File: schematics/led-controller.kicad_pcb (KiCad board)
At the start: 2 copper layers, 58 parts, among them IC1 ATMEGA168A-P, P1 CONN_01X03, P2 CONN_01X03, P3 CONN_01X02, P4 CONN_01X02, P5 CONN_01X02, P6 CONN_01X02, P7 ISP, P8 COM, Q1 IRLU 120N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

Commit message: first checked version
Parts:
- removed JP1: Jumper_NO_Small, Pin_Headers:Pin_Header_Straight_1x02
- added C10: 100n, Capacitors_ThroughHole:C_Rect_L7_W2.5_P5, F.Cu at (103.9, 101.9)
- added C11: 100n, Capacitors_ThroughHole:C_Rect_L7_W2.5_P5, F.Cu at (158.0, 74.2)
- added CON1: BARREL_JACK, Connect:BARREL_JACK, F.Cu at (172.5, 105.4)
- added D6: 1N5408, Diodes_ThroughHole:Diode_DO-201AD_Horizontal_RM15, F.Cu at (176.3, 87.4)
- added F1: 3A, Fuse_Holders_and_Fuses:Fuseholder5x20_horiz_open_lateral_Type-II, F.Cu at (168.4, 85.1)
- added REF**: MountingHole_3.2mm_M3, Mounting_Holes:MountingHole_3.2mm_M3, F.Cu at (99.1, 121.9)
- added REF**: MountingHole_3.2mm_M3, Mounting_Holes:MountingHole_3.2mm_M3, F.Cu at (99.1, 38.1)
- added REF**: MountingHole_3.2mm_M3, Mounting_Holes:MountingHole_3.2mm_M3, F.Cu at (172.7, 38.1)
- added REF**: MountingHole_3.2mm_M3, Mounting_Holes:MountingHole_3.2mm_M3, F.Cu at (172.7, 121.9)
- C1, C2, C3, C4: footprint Capacitors_ThroughHole:C_Radial_D5_L11_P2.5 -> Capacitors_ThroughHole:C_Radial_D8_L11.5_P3.5
- P1: value CONN_01X03 -> VIN
- P2: value CONN_01X03 -> VOUT
- P3: value CONN_01X02 -> LED1; footprint Connect:AK300-2 -> Connect:bornier2
- P4, P5, P6: footprint Connect:AK300-2 -> Connect:bornier2
- P7: footprint Socket_Strips:Socket_Strip_Straight_2x03 -> Pin_Headers:Pin_Header_Straight_2x03
- RR4: value 20k -> 27k
- RV1, RV2, RV3, RV4: footprint Potentiometers:Potentiometer_Trimmer-Suntan-TSR-3386C -> Trimmers:Potentiometer_Trimmer-Suntan-TSR-3296
- U3: value LF33CV -> LP 2950 ACZ3,3; footprint TO_SOT_Packages_THT:TO-220_Neutral123_Vertical -> TO_SOT_Packages_THT:TO-92_Inline_Narrow_Oval
- moved C5 49.3 mm to (103.9, 80.5)
- moved C7 40.3 mm to (148.1, 102.9), turned to 270 degrees
- moved C6 34.8 mm to (134.9, 77.5), turned to 180 degrees
- moved P1 34.1 mm to (161.0, 117.6), turned to 90 degrees
- moved C8 30.1 mm to (151.6, 108.0), turned to 90 degrees
- moved C9 23.3 mm to (103.9, 112.3), turned to 270 degrees
- moved RR3 15.5 mm to (109.5, 91.4)
- moved P2 14.0 mm to (161.0, 113.3), turned to 90 degrees
- moved P8 4.33 mm to (161.0, 122.7), turned to 90 degrees
- moved C1 3.56 mm to (101.3, 67.1)
- moved Q4 3.56 mm to (173.7, 67.1)
- moved U3 2.59 mm to (156.7, 102.9)
- moved P4 2.55 mm to (126.7, 36.6), turned to 180 degrees
- moved P5 2.55 mm to (145.0, 36.6), turned to 180 degrees
- moved P6 2.55 mm to (163.3, 36.6), turned to 180 degrees
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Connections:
- C6 pad 1: +3V3 -> VCC
- C7 pad 1: +3V3 -> VCC
- IC1 pad 25: SENSE2 -> SENSE1
- IC1 pad 26: SENSE1 -> SENSE2
- P1 pad 2: Net-(JP1-Pad1) -> +3V3
- P2 pad 2: Net-(JP1-Pad1) -> +3V3
- P3 pad 1: /IRAW1 -> Net-(L1-Pad1)
- P3 pad 2: Net-(L1-Pad1) -> /IRAW1
- P4 pad 1: /IRAW2 -> Net-(L2-Pad1)
- P4 pad 2: Net-(L2-Pad1) -> /IRAW2
- P5 pad 1: /IRAW3 -> Net-(L3-Pad1)
- P5 pad 2: Net-(L3-Pad1) -> /IRAW3
- P6 pad 1: /IRAW4 -> Net-(L4-Pad1)
- P6 pad 2: Net-(L4-Pad1) -> /IRAW4
- RR3 pad 2: /PULLUP1 -> /PULLUP2
- RR3 pad 3: /PULLUP2 -> /PULLUP1
- RR3 pad 4: /PULLUP3 -> /PULLUP4
- RR3 pad 5: /PULLUP4 -> /PULLUP3
- U2 pad 1: /PULLUP1 -> (no net)
- U2 pad 10: (no net) -> SENSE1
- U2 pad 11: (no net) -> /PULLUP1
- U2 pad 12: (no net) -> SENSE2
- U2 pad 13: (no net) -> /PULLUP2
- U2 pad 2: SENSE1 -> (no net)
- U2 pad 3: /PULLUP2 -> (no net)
- U2 pad 4: SENSE2 -> (no net)
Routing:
- net Net-(JP1-Pad1): track 58.6 -> 0.00 mm
- net Net-(CON1-Pad1): track 0.00 -> 18.7 mm
- net +3V3: track 135.3 -> 152.8 mm
- net /PULLUP2: track 26.6 -> 9.94 mm
- net Net-(D6-Pad2): track 0.00 -> 12.6 mm
- net /PULLUP1: track 22.4 -> 11.0 mm
- net /PULLUP4: track 34.4 -> 23.1 mm
- net SWITCH4: track 29.3 -> 39.5 mm
- net SENSE2: track 67.3 -> 76.0 mm
- net MOSI: track 12.8 -> 19.5 mm
- net VCC: track 197.5 -> 203.0 mm
- net SCK: track 19.5 -> 14.2 mm
- net SENSE1: track 78.4 -> 82.9 mm
- net SWITCH2: track 39.6 -> 35.9 mm
- net MISO: track 17.6 -> 14.1 mm
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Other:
- board outline added: 88.9 x 97.8 mm
- board text added: "4 Channel LED Driver, (c) Andreas Stöckel, 2016 max. 0.9A per channel, 3A total"
- board text added: "DC IN 5-25V"
- board text added: "RX"
- board text added: "TX"
- board text added: "UART"
- board text added: "VIN"
- board text added: "VOUT"

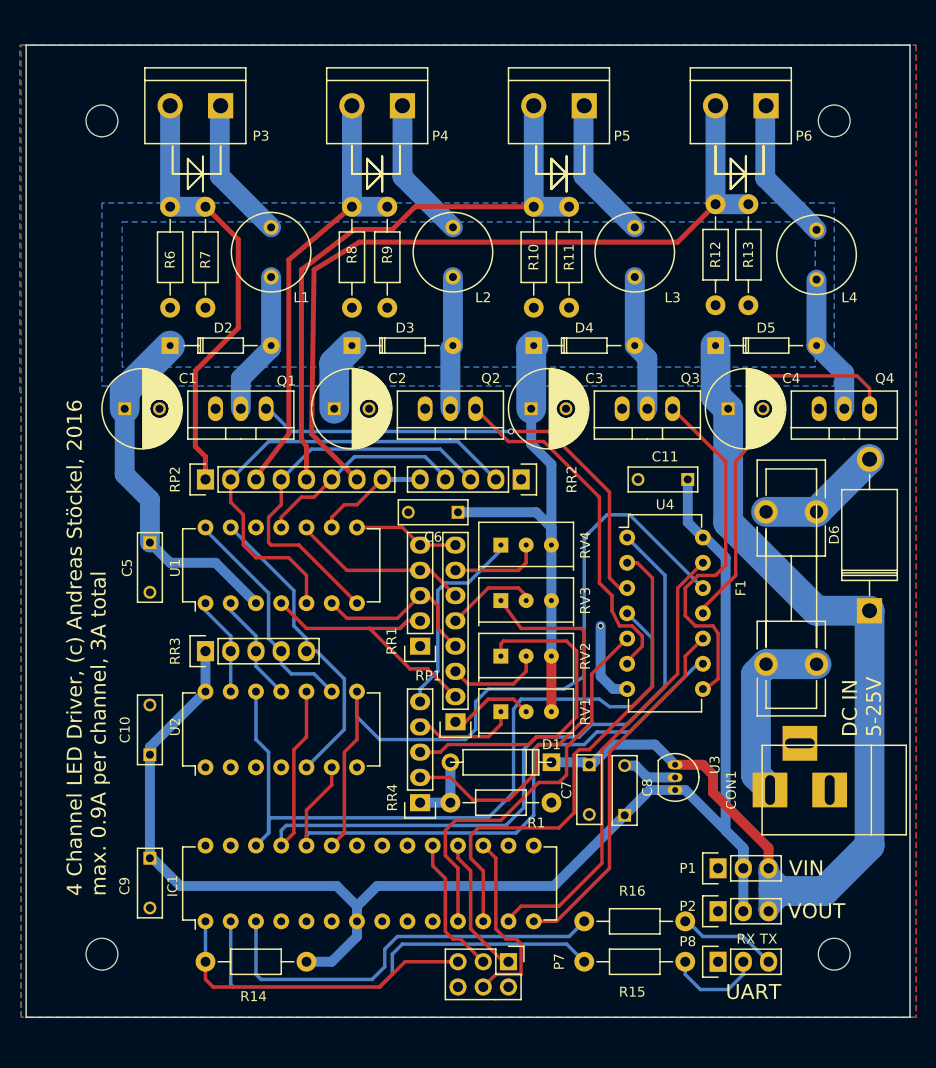
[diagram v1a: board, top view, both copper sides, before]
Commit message: Improve PCB
- Move mounting holes to 71.5mm distance, allows to attach the board to a
  80mm fan
- Improve ground planes, remove one via
- Prettify some tracks
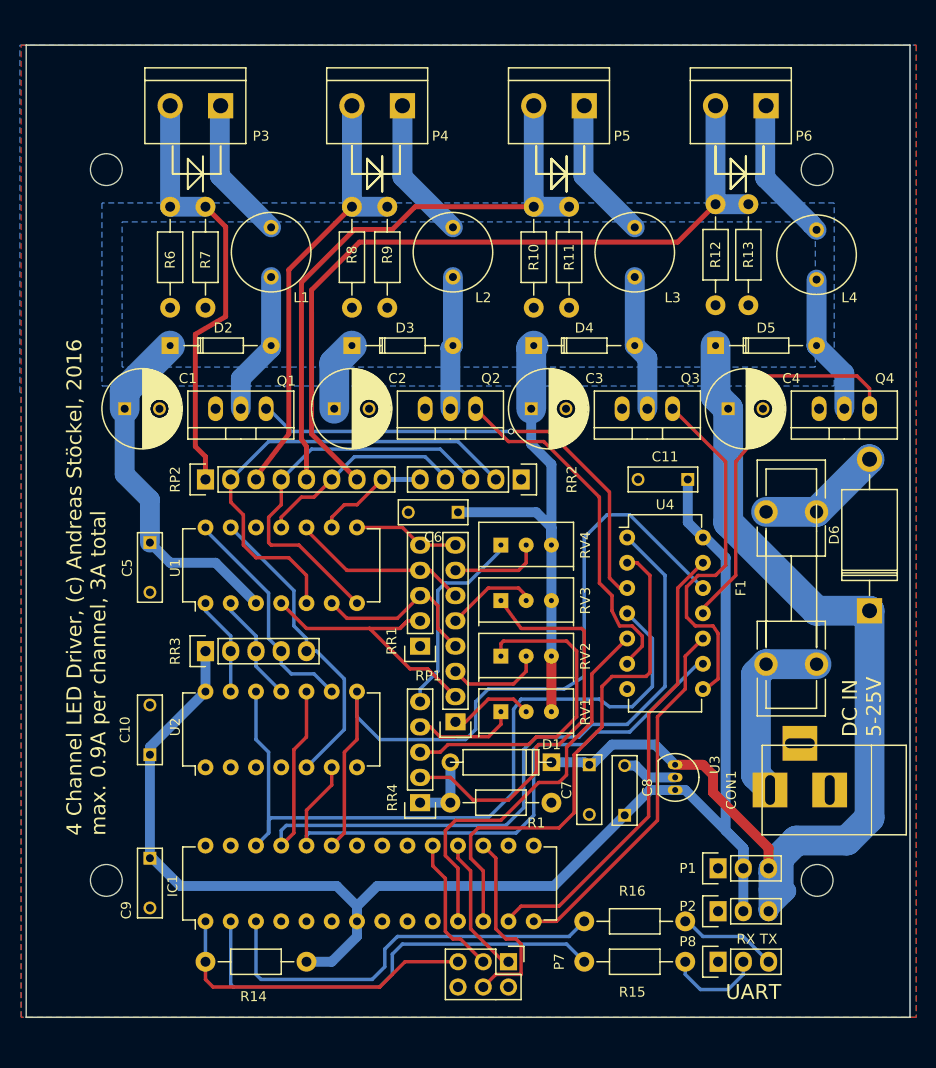
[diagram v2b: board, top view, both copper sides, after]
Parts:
- moved REF** 7.62 mm to (171.0, 114.5)
- moved REF** 7.43 mm to (99.5, 114.5)
- moved REF** 5.19 mm to (171.0, 43.0)
- moved REF** 4.92 mm to (99.5, 43.0)
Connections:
- U2 pad 1: (no net) -> GND
- U2 pad 2: (no net) -> Net-(U2-Pad2)
- U2 pad 3: (no net) -> GND
- U2 pad 4: (no net) -> Net-(U2-Pad4)
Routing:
- net GND: track 13.8 -> 5.57 mm, vias 1 -> 0
- net TRIGGER1: track 51.2 -> 52.5 mm
- net /IRAW4: track 78.7 -> 78.1 mm
- net /IRAW1: track 44.7 -> 44.2 mm
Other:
- board text removed: "VIN"
- board text removed: "VOUT"

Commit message: Board version 1.0 RC1
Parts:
- removed D1: 3V6, Discret:D4
- removed D6: 1N5408, Diodes_ThroughHole:Diode_DO-201AD_Horizontal_RM15
- removed R1: 1k, Resistors_ThroughHole:Resistor_Horizontal_RM10mm
- added C12: 100n, Capacitors_ThroughHole:C_Rect_L7_W2.5_P5, F.Cu at (138.6, 105.5)
- added C13: 100n, Capacitors_ThroughHole:C_Rect_L7_W2.5_P5, F.Cu at (127.3, 105.5)
- added P9: EXPANSION, Pin_Headers:Pin_Header_Straight_1x04, F.Cu at (106.9, 105.5)
- added U5: 7905_wno, TO_SOT_Packages_THT:TO-92_Inline_Narrow_Oval, F.Cu at (124.2, 89.9)
- D2, D3, D4, D5: value SD101C -> 1N5819
- P1, P2, P8: footprint Pin_Headers:Pin_Header_Straight_1x03 -> Connect:PINHEAD1-3
- R14, R15, R16: footprint Resistors_ThroughHole:Resistor_Horizontal_RM10mm -> Discret:R1
- RP1, RP2, RR1, RR2, RR3: value 10k -> 100k
- RR4: value 27k -> 4.7k
- RV1, RV2, RV3, RV4: value 10k -> 1k
- moved P8 48.9 mm to (112.1, 122.7), turned to 0 degrees
- moved R15 37.0 mm to (120.8, 122.9), turned to 90 degrees
- moved R16 32.2 mm to (125.9, 122.9), turned to 90 degrees
- moved R14 11.2 mm to (130.8, 122.9), turned to 90 degrees
- moved P2 10.9 mm to (155.4, 122.7), turned to 0 degrees
- moved P1 6.19 mm to (155.4, 114.9), turned to 0 degrees
- moved C7 5.02 mm to (152.9, 101.5), turned to 0 degrees
- moved U3 3.68 mm to (154.2, 105.5), turned to 0 degrees
- moved C8 1.80 mm to (152.9, 109.2), turned to 0 degrees
- moved CON1 1.78 mm to (172.5, 103.6)
- moved C1 1.14 mm to (101.3, 65.9)
- moved C10 1.14 mm to (103.9, 100.7)
- moved C11 1.14 mm to (158.0, 73.0)
- moved C2 1.14 mm to (122.4, 65.9)
- moved C3 1.14 mm to (142.2, 65.9)
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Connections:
- F1 pad 2: Net-(D6-Pad2) -> VCC
- IC1 pad 20: Net-(IC1-Pad20) -> +3V3
- IC1 pad 27: Net-(IC1-Pad27) -> /E4
- IC1 pad 28: Net-(IC1-Pad28) -> /E2
- IC1 pad 4: Net-(IC1-Pad4) -> /E1
- IC1 pad 5: Net-(IC1-Pad5) -> /E3
- R14 pad 1: +3V3 -> RESET
- R14 pad 2: RESET -> +3V3
- RR4 pad 1: Net-(D1-Pad2) -> /-5V
- U1 pad 10: REF3 -> ISENSE3
- U1 pad 11: ISENSE3 -> REF3
- U1 pad 4: REF1 -> ISENSE1
- U1 pad 5: ISENSE1 -> REF1
- U1 pad 6: REF2 -> ISENSE2
- U1 pad 7: ISENSE2 -> REF2
- U1 pad 8: REF4 -> ISENSE4
- U1 pad 9: ISENSE4 -> REF4
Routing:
- net GND: track 5.57 -> 48.4 mm
- net Net-(IC1-Pad2): track 45.7 -> 11.8 mm
- net Net-(IC1-Pad3): track 42.0 -> 13.6 mm
- net /-5V: track 0.00 -> 25.7 mm, vias 0 -> 1
- net /IRAW4: track 78.1 -> 98.9 mm
- net /E1: track 0.00 -> 20.5 mm
- net /E3: track 0.00 -> 20.4 mm
- net /IRAW3: track 60.0 -> 79.0 mm
- net VCC: track 203.3 -> 219.2 mm
- net /IRAW2: track 44.6 -> 60.2 mm
- net Net-(D6-Pad2): track 12.6 -> 0.00 mm
- net Net-(RR4-Pad3): track 33.5 -> 21.9 mm
- net SENSE4: track 76.9 -> 86.8 mm
- net Net-(RR4-Pad2): track 41.4 -> 33.1 mm
- net Net-(D1-Pad2): track 7.37 -> 0.00 mm
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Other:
- board text added: "DC IN 6-25V"
- board text added: "ISP"
- board text removed: "DC IN 5-25V"

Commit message: Led Controller RC2
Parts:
- added C14: 1u, Capacitors_ThroughHole:C_Radial_D5_L6_P2.5, F.Cu at (148.2, 117.5)
- added C15: 1u, Capacitors_ThroughHole:C_Radial_D5_L6_P2.5, F.Cu at (136.7, 102.1)
- RP1, RP2: footprint Pin_Headers:Pin_Header_Straight_1x08 -> w_pth_resistors:r-sil_8
- RR1, RR2, RR3, RR4: footprint Pin_Headers:Pin_Header_Straight_1x05 -> w_pth_resistors:r-sil_5
- moved RP1 8.89 mm to (134.6, 88.5), turned to 90 degrees
- moved RP2 8.89 mm to (118.4, 73.0), turned to 0 degrees
- moved RR4 5.08 mm to (131.1, 100.5), turned to 90 degrees
- moved RR1 5.08 mm to (131.1, 84.7), turned to 90 degrees
- moved RR3 5.08 mm to (114.6, 90.3), turned to 0 degrees
- moved RR2 5.08 mm to (136.1, 73.0), turned to 180 degrees
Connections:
- IC1 pad 10: Net-(IC1-Pad10) -> (no net)
- IC1 pad 15: Net-(IC1-Pad15) -> (no net)
- IC1 pad 16: Net-(IC1-Pad16) -> (no net)
- IC1 pad 6: Net-(IC1-Pad6) -> (no net)
- IC1 pad 9: Net-(IC1-Pad9) -> (no net)
- P7 pad 2: Net-(P7-Pad2) -> (no net)
- U2 pad 2: Net-(U2-Pad2) -> (no net)
- U2 pad 4: Net-(U2-Pad4) -> (no net)
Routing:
- net +3V3: track 149.6 -> 160.6 mm
- net VCC: track 219.2 -> 227.6 mm
- net /-5V: track 25.7 -> 31.3 mm, vias 1 -> 0
- net /PULLUP2: track 11.5 -> 10.7 mm
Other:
- board text added: "DC IN 7-25V"
- board text removed: "DC IN 6-25V"

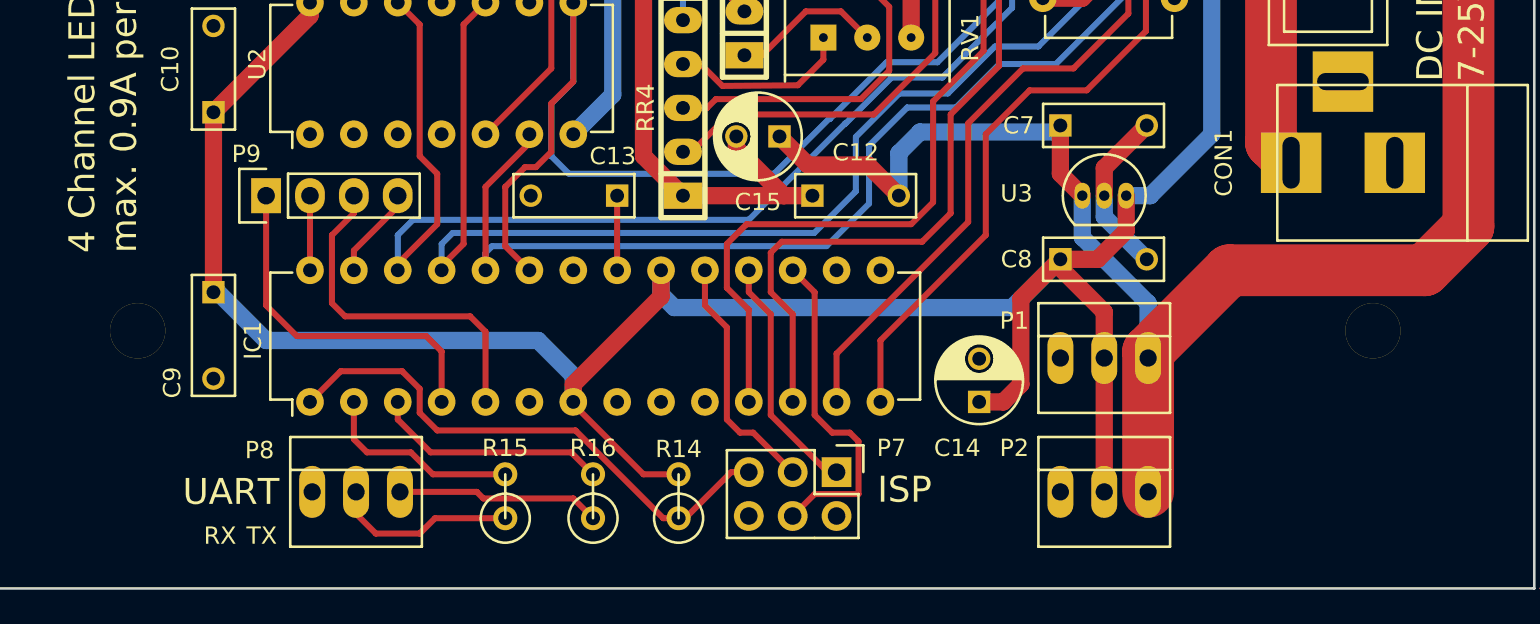
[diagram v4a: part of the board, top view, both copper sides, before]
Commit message: RC3 -- Connected all pins to PWM outputs
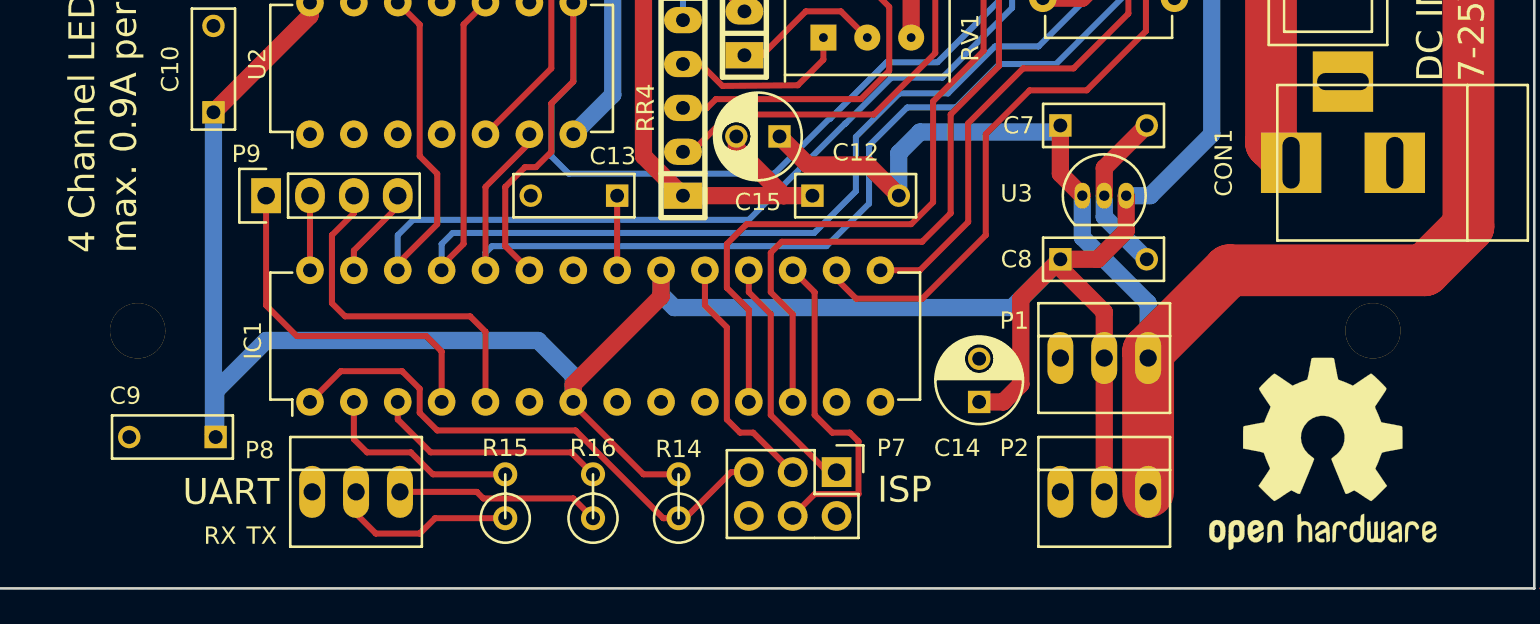
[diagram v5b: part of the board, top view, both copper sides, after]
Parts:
- added REF***: OSHW-Logo2_14.6x12mm_SilkScreen, Symbols:OSHW-Logo2_14.6x12mm_SilkScreen, F.Cu at (168.1, 120.5)
- moved C9 8.38 mm to (104.0, 119.5), turned to 180 degrees
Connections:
- IC1 pad 13: TRIGGER4 -> (no net)
- IC1 pad 14: TRIGGER3 -> (no net)
- IC1 pad 15: (no net) -> TRIGGER4
- IC1 pad 16: (no net) -> TRIGGER3
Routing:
- net +3V3: track 160.6 -> 171.6 mm
- net TRIGGER4: track 47.6 -> 39.5 mm
- net TRIGGER3: track 38.2 -> 36.4 mm
